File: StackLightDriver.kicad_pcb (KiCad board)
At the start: 2 copper layers, 74 parts, among them J1 B2B-XH-A, J10 B2B-XH-A, J11 PJ-102AH, J2 B2B-XH-A, J3 B2B-XH-A, J4 B2B-XH-A, J5 B2B-XH-A, J6 B2B-XH-A, J7 B2B-XH-A, J8 B2B-XH-A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

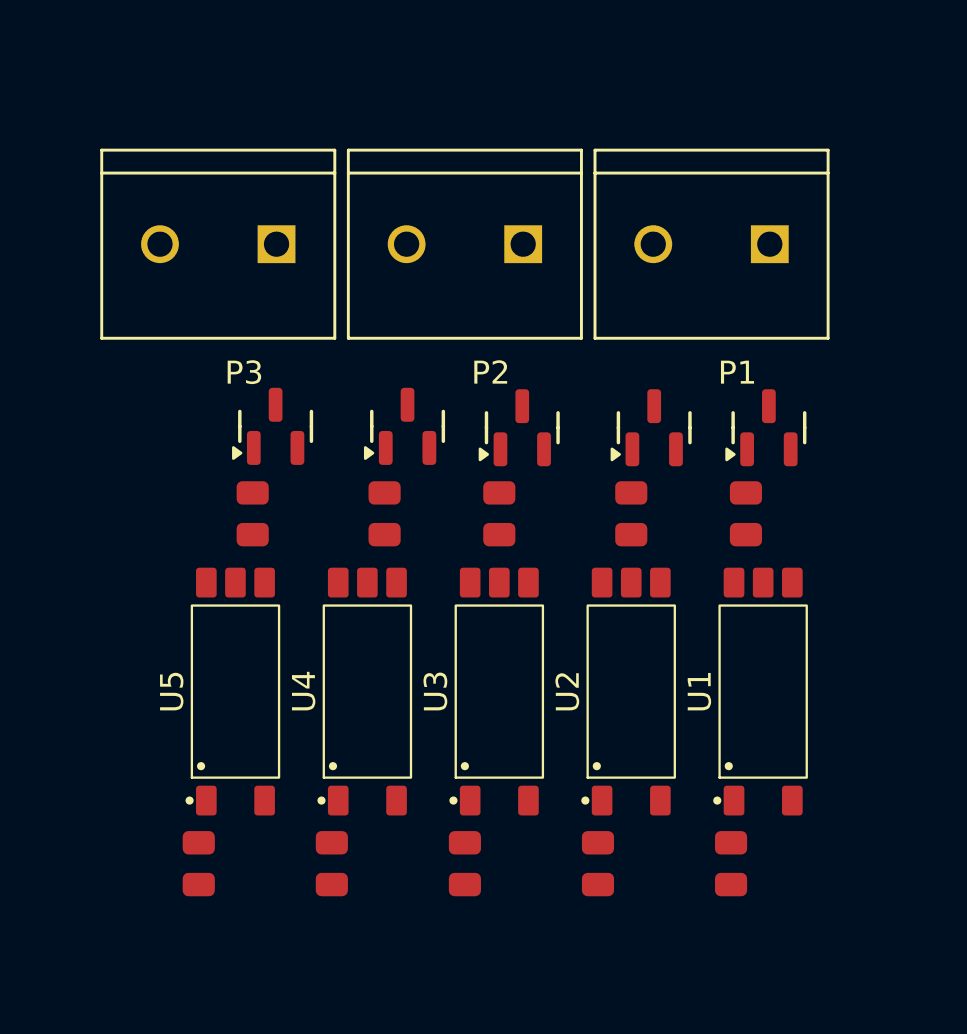
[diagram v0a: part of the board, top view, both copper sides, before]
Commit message: Added fuse models, LTV5314 models (Just step files for now)
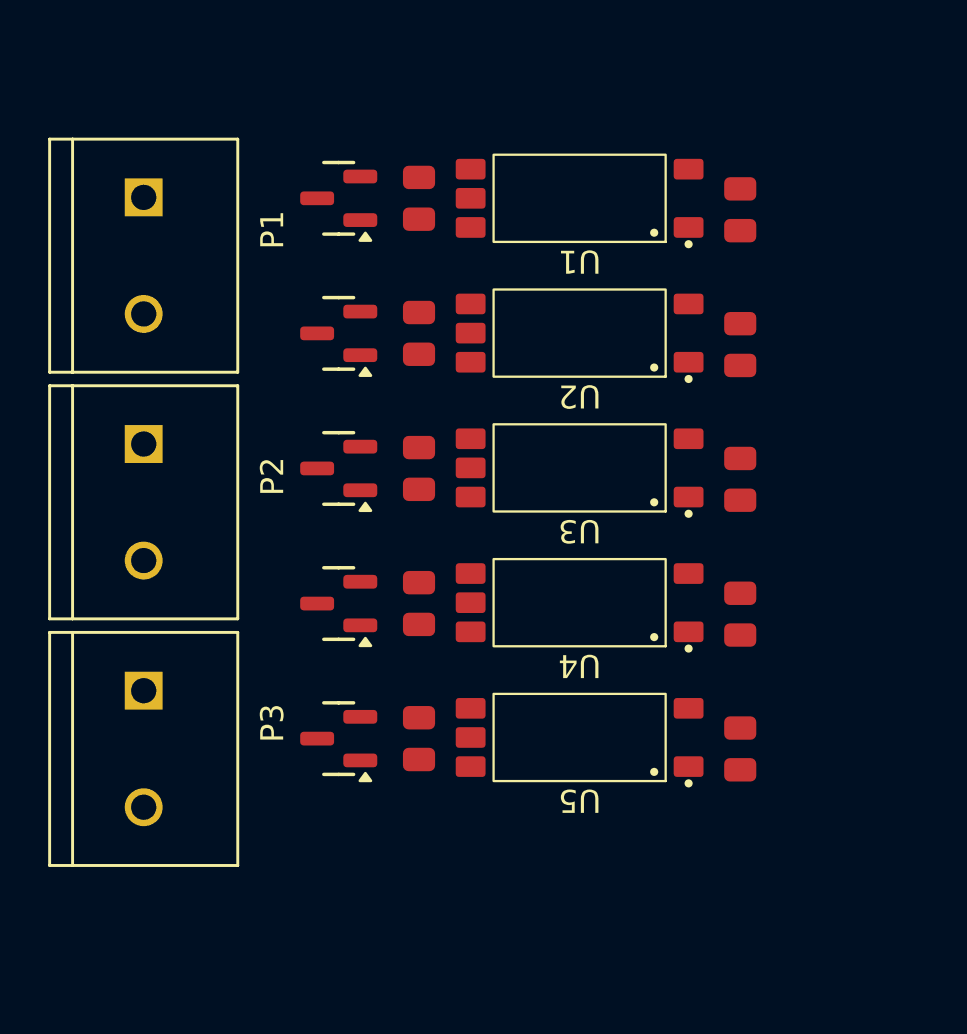
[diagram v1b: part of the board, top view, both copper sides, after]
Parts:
- moved R11 28.5 mm to (90.5, 39.2), turned to -90 degrees
- moved P1 24.8 mm to (64.5, 41.2), turned to -90 degrees
- moved R15 24.1 mm to (90.5, 62.8), turned to -90 degrees
- moved R12 23.5 mm to (90.5, 45.1), turned to -90 degrees
- moved U1 22.9 mm to (83.5, 38.8), turned to 180 degrees
- moved P3 22.2 mm to (64.5, 62.8), turned to -90 degrees
- moved Q1 21.2 mm to (73.0, 38.8), turned to 180 degrees
- moved R14 20.9 mm to (90.5, 56.9), turned to -90 degrees
- moved R13 20.6 mm to (90.5, 51.0), turned to -90 degrees
- moved R16 19.8 mm to (76.5, 38.8)
- moved P2 18.0 mm to (64.5, 52.0), turned to -90 degrees
- moved U2 15.8 mm to (83.5, 44.6), turned to 180 degrees
- moved U5 15.1 mm to (83.5, 62.2), turned to 180 degrees
- moved Q2 14.4 mm to (73.0, 44.6), turned to 180 degrees
- moved Q5 13.9 mm to (73.0, 62.3), turned to 180 degrees
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
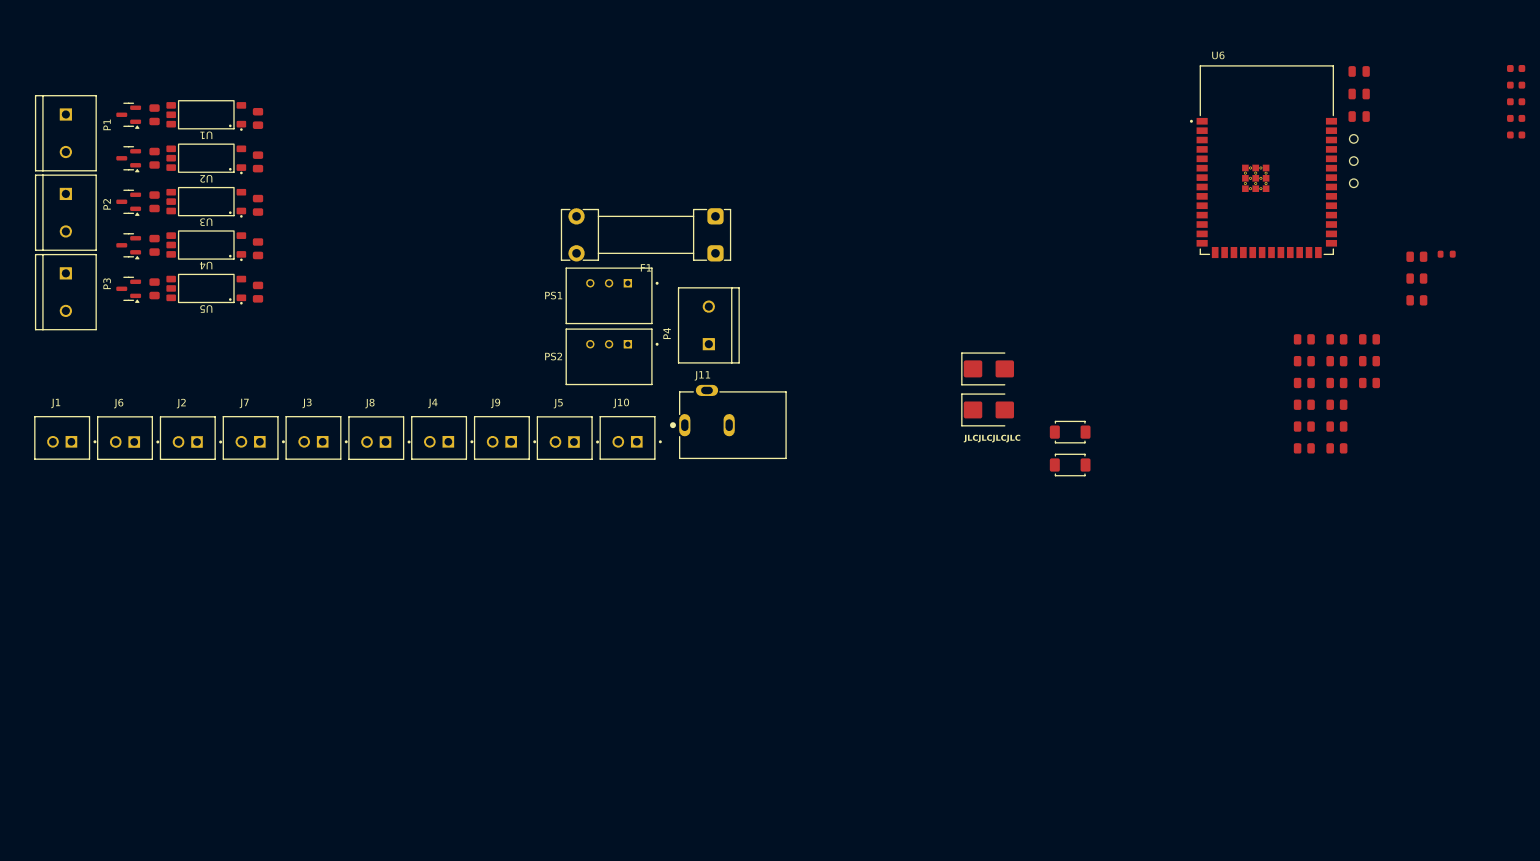
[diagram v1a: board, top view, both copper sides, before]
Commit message: Rearranged components slightly, situating ESP32 better
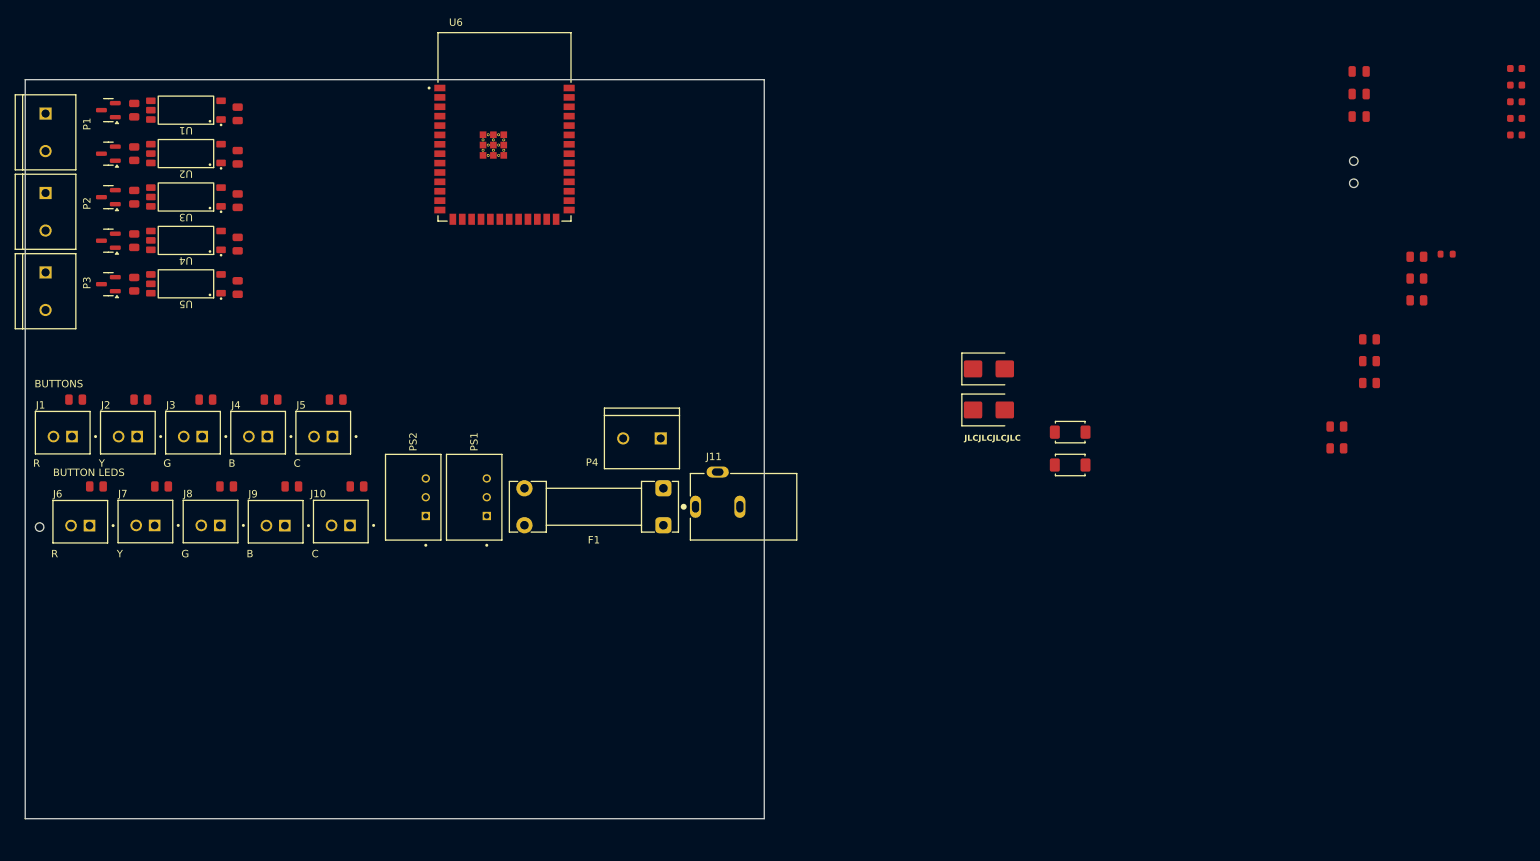
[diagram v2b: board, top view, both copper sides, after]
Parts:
- moved H1 185.4 mm to (61.0, 94.5)
- moved R1 166.4 mm to (65.8, 77.3), turned to 180 degrees
- moved R6 163.5 mm to (68.6, 89.0)
- moved R7 160.3 mm to (77.5, 89.0)
- moved R2 157.5 mm to (74.6, 77.3), turned to 180 degrees
- moved R8 151.2 mm to (86.3, 89.0)
- moved R3 148.6 mm to (83.5, 77.3), turned to 180 degrees
- moved R9 142.1 mm to (95.1, 89.0)
- moved R4 139.8 mm to (92.3, 77.3), turned to 180 degrees
- moved R10 133.1 mm to (103.9, 89.0)
- moved R5 131.1 mm to (101.1, 77.3), turned to 180 degrees
- moved U6 103.2 mm to (123.8, 40.4)
- moved J10 40.4 mm to (101.7, 93.8)
- moved F1 37.5 mm to (145.3, 94.3)
- moved PS1 32.8 mm to (119.8, 90.5), turned to 90 degrees
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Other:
- board outline added: 100 x 100 mm
- board text added: "B"
- board text added: "BUTTON LEDS"
- board text added: "BUTTONS"
- board text added: "C"
- board text added: "G"
- board text added: "R"
- board text added: "Y"

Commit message: Added models and footprint for Adafruit Max98357
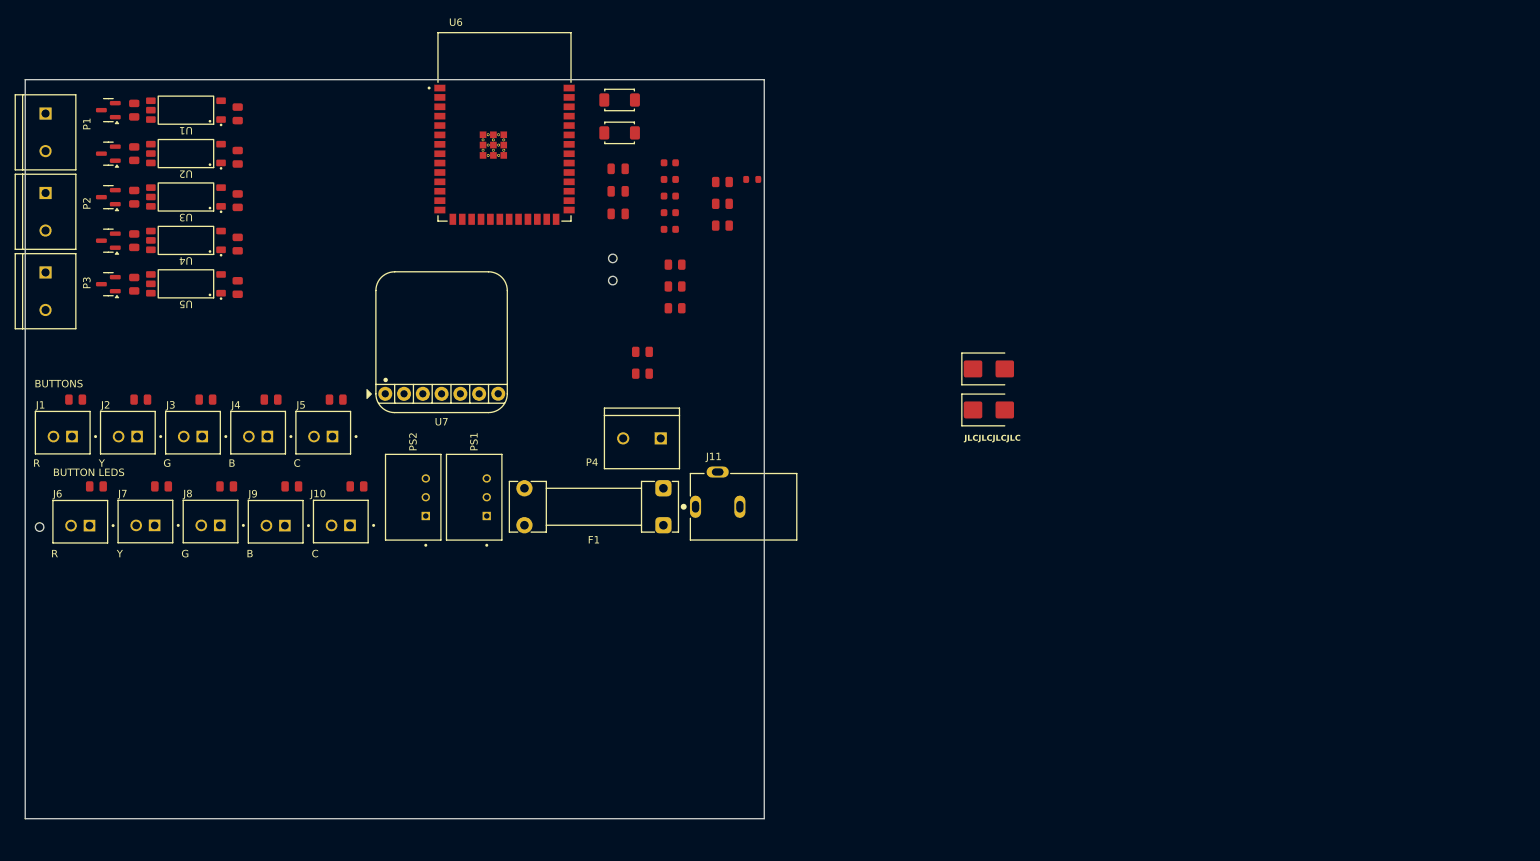
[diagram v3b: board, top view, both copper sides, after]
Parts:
- added U7: MAX98357A, Project_footprints:Adafruit_I2S_MAX98357A, F.Cu at (115.3, 76.5)
- moved C1 115.2 mm to (146.2, 45.2)
- moved C2 115.2 mm to (146.2, 47.5)
- moved C3 115.2 mm to (146.2, 49.8)
- moved C4 115.2 mm to (146.2, 52.0)
- moved C5 115.2 mm to (146.2, 54.2)
- moved C6 101.1 mm to (139.2, 46.1)
- moved C7 101.1 mm to (139.2, 49.1)
- moved C8 101.1 mm to (139.2, 52.2)
- moved H2 101.1 mm to (138.5, 58.2)
- moved H3 101.1 mm to (138.5, 61.2)
- moved R21 94.5 mm to (142.5, 70.8)
- moved R22 94.5 mm to (142.5, 73.8)
- moved R23 94.5 mm to (146.9, 59.0)
- moved R24 94.5 mm to (153.3, 47.9)
- moved R25 94.5 mm to (153.3, 50.8)
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
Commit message: Added some TVS diodes to schematic and to PCB layout
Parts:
- added D10: H3V3L10B, PCM_JLCPCB:D_DFN1006-2L, F.Cu at (183.2, 107.8)
- added D11: H3V3L10B, PCM_JLCPCB:D_DFN1006-2L, F.Cu at (183.2, 109.4)
- added D12: H3V3L10B, PCM_JLCPCB:D_DFN1006-2L, F.Cu at (183.2, 111.1)
- added D13: H3V3L10B, PCM_JLCPCB:D_DFN1006-2L, F.Cu at (185.5, 102.8)
- added D14: H3V3L10B, PCM_JLCPCB:D_DFN1006-2L, F.Cu at (185.5, 104.5)
- added D15: H3V3L10B, PCM_JLCPCB:D_DFN1006-2L, F.Cu at (185.5, 106.1)
- added D16: SMF14CA, PCM_JLCPCB:D_SOD-123FL, F.Cu at (69.0, 59.0)
- added D17: SMF14CA, PCM_JLCPCB:D_SOD-123FL, F.Cu at (69.0, 54.5)
- added D18: SMF14CA, PCM_JLCPCB:D_SOD-123FL, F.Cu at (69.0, 48.5)
- added D19: SMF14CA, PCM_JLCPCB:D_SOD-123FL, F.Cu at (69.0, 43.5)
- added D20: SMF14CA, PCM_JLCPCB:D_SOD-123FL, F.Cu at (69.0, 37.5)
- added D21: SMF14CA, PCM_JLCPCB:D_SOD-123FL, F.Cu at (137.0, 118.1)
- added D3: H3V3L10B, PCM_JLCPCB:D_DFN1006-2L, F.Cu at (180.9, 106.1)
- added D4: H3V3L10B, PCM_JLCPCB:D_DFN1006-2L, F.Cu at (180.9, 107.8)
- added D5: H3V3L10B, PCM_JLCPCB:D_DFN1006-2L, F.Cu at (180.9, 109.4)
- added D6: H3V3L10B, PCM_JLCPCB:D_DFN1006-2L, F.Cu at (180.9, 111.1)
- added D7: H3V3L10B, PCM_JLCPCB:D_DFN1006-2L, F.Cu at (183.2, 102.8)
- added D8: H3V3L10B, PCM_JLCPCB:D_DFN1006-2L, F.Cu at (183.2, 104.5)
- added D9: H3V3L10B, PCM_JLCPCB:D_DFN1006-2L, F.Cu at (183.2, 106.1)
- added U8: USBLC6-2SC6, Package_TO_SOT_SMD:SOT-23-6, F.Cu at (182.4, 114.3)
- D1, D2: value SMBJ3.3CA -> H3V3L10B; footprint PCM_JLCPCB:D_SMB -> PCM_JLCPCB:D_DFN1006-2L
- moved D1 30.9 mm to (180.9, 102.8)
- moved D2 27.1 mm to (180.9, 104.5)
- moved Q1 4.19 mm to (74.0, 40.0)
- moved Q2 4.19 mm to (74.0, 45.9)
- moved Q3 4.19 mm to (74.0, 51.8)
- moved Q4 4.19 mm to (74.0, 57.7)
- moved Q5 4.19 mm to (74.0, 63.5)
- moved R11 4.19 mm to (91.5, 40.5)
- moved R12 4.19 mm to (91.5, 46.4)
- moved R13 4.19 mm to (91.5, 52.2)
- moved R14 4.19 mm to (91.5, 58.1)
- moved R15 4.19 mm to (91.5, 64.0)
- moved R16 4.19 mm to (77.5, 40.0)
- moved R17 4.19 mm to (77.5, 45.9)
- moved R18 4.19 mm to (77.5, 51.8)
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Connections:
- D1 pad 2: /D- -> VMCU
- D2 pad 2: /D+ -> VMCU

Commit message: Added footprint for USB-C receptacle
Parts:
- added J12: USB_C_Receptacle_USB2.0_14P, Project_footprints:USB_C_Receptacle_USB2.0_14P, F.Cu at (102.8, 43.5)
- added Q6: HL2303, PCM_JLCPCB:Q_SOT-23, F.Cu at (130.5, 83.0)
- added R30: 5.1kΩ, PCM_JLCPCB:R_0805, F.Cu at (99.4, 48.1)
- added R31: 10kΩ, PCM_JLCPCB:R_0805, F.Cu at (99.4, 51.0)
- moved D21 39.8 mm to (133.0, 78.5)
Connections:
- D21 pad 1: Net-(D21-Pad1) -> Net-(Q6-D)
- F1 pad 1: Net-(D21-Pad1) -> Net-(F1-Pad1)
- F1 pad 2: VSupply -> Net-(F1-Pad2)
- J11 pad 2: Net-(J11-Pad2) -> Net-(F1-Pad1)
- J11 pad 3: Net-(J11-Pad2) -> Net-(F1-Pad1)
- P4 pad 1: Net-(J11-Pad2) -> Net-(F1-Pad2)
- P4 pad 2: Net-(D21-Pad1) -> Net-(Q6-D)
- U8 pad 5: unconnected-(U8-VBUS-Pad5) -> Net-(U8-VBUS)
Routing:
- added copper zone on B.Cu, net GND

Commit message: Fixed incorrect decoupling capacitance on LTV5314
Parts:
- C1, C2, C3, C4, C5: value 1uF -> 100nF; footprint PCM_JLCPCB:C_0603 -> PCM_JLCPCB:C_0805
- moved C5 67.1 mm to (80.8, 69.0)
- moved C4 66.2 mm to (80.8, 62.0)
- moved C3 65.7 mm to (80.8, 55.2)
- moved C1 65.6 mm to (80.8, 41.5)
- moved C2 65.5 mm to (80.8, 48.2)
- moved Q5 2.50 mm to (74.1, 66.0)
- moved R20 2.45 mm to (77.5, 66.0)
- moved R11 2.25 mm to (91.5, 38.2)
- moved Q1 2.05 mm to (74.1, 38.0)
- moved U5 2.02 mm to (84.2, 65.5)
- moved R15 2.00 mm to (91.5, 66.0)
- moved R16 2.00 mm to (77.5, 38.0)
- moved U1 2.00 mm to (84.5, 38.0)
- moved D19 1.50 mm to (69.0, 45.0)
- moved Q4 1.36 mm to (74.0, 59.0)
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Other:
- board text added: "+"
- board text added: "-"

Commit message: Placed TVS diodes on board
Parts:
- moved D6 122.1 mm to (63.5, 77.5), turned to -90 degrees
- moved D11 115.7 mm to (69.2, 89.8), turned to -90 degrees
- moved D1 115.5 mm to (68.2, 77.5), turned to -90 degrees
- moved D7 113.8 mm to (72.3, 77.5), turned to -90 degrees
- moved D2 107.3 mm to (77.1, 77.5), turned to -90 degrees
- moved D12 107.1 mm to (78.2, 89.8), turned to -90 degrees
- moved D8 105.6 mm to (81.1, 77.5), turned to -90 degrees
- moved U8 100.0 mm to (105.0, 51.0)
- moved D13 99.4 mm to (87.0, 89.8), turned to -90 degrees
- moved D3 99.3 mm to (85.9, 77.5), turned to -90 degrees
- moved D9 97.6 mm to (89.9, 77.5), turned to -90 degrees
- moved D4 91.4 mm to (94.7, 77.5), turned to -90 degrees
- moved D14 91.0 mm to (95.8, 89.8), turned to -90 degrees
- moved D10 89.7 mm to (98.8, 77.5), turned to -90 degrees
- moved D5 83.8 mm to (103.5, 77.5), turned to -90 degrees
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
